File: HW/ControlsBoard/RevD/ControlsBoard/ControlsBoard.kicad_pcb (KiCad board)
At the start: 2 copper layers, 54.6 x 21.8 mm, 12 parts, among them J1 Conn_01x12, SW1 Rotary_Encoder_Switch, SW2 SW_SPST, SW3 SW_SPST, SW4 SW_SPST, SW5 SW_SPST

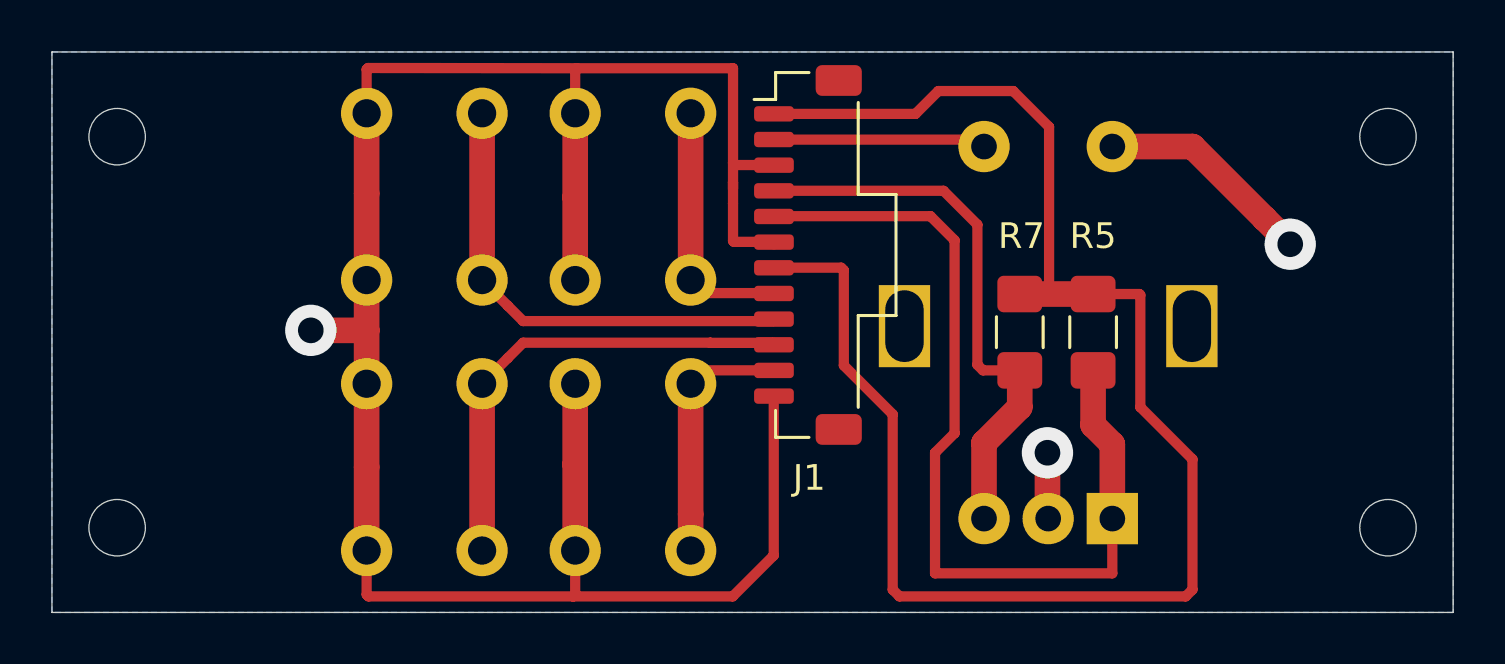
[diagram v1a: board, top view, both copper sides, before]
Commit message: updated front panel svg
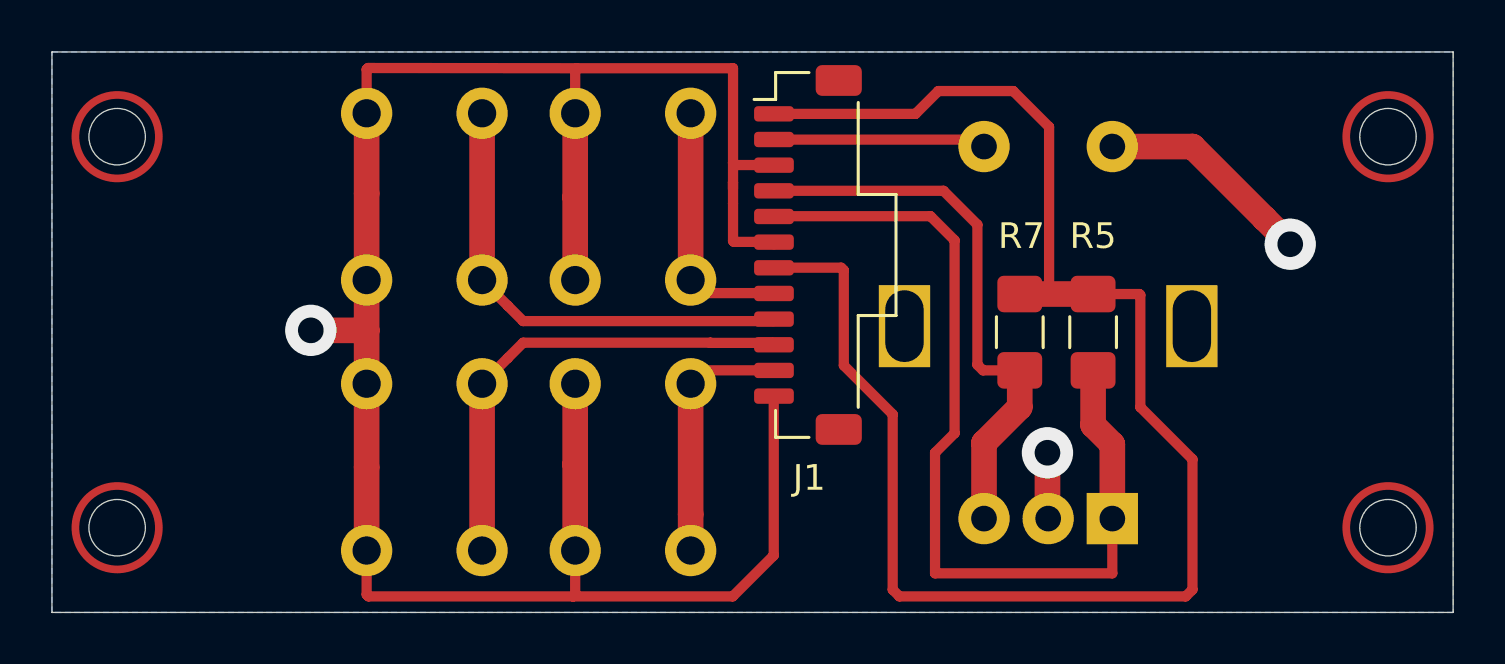
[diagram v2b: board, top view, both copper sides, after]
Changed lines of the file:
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@@
-(kicad_pcb (version 20171130) (host pcbnew "(5.1.5-0-10_14)")
+(kicad_pcb (version 20171130) (host pcbnew 5.1.5-52549c5~86~ubuntu18.04.1)
   (general
     (thickness 1.6)
-    (drawings 4)
+    (drawings 8)
     (tracks 113)
     (zones 0)
@@
     )
   )
+  (gr_circle (center 116.84 53.34) (end 118.466394 53.34) (layer F.Cu) (width 0.3))
+  (gr_circle (center 116.84 68.58) (end 118.466394 68.58) (layer F.Cu) (width 0.3))
+  (gr_circle (center 166.37 68.58) (end 167.996394 68.58) (layer F.Cu) (width 0.3))
+  (gr_circle (center 166.37 53.34) (end 167.996394 53.34) (layer F.Cu) (width 0.3))
   (gr_line (start 168.91 71.882) (end 168.91 50.038) (layer Edge.Cuts) (width 0.05))
   (gr_line (start 114.3 71.882) (end 114.3 50.038) (layer Edge.Cuts) (width 0.05))
